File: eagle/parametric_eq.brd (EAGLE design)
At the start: 100 x 80 mm, 39 parts, among them IC1 TL072P, IC2 TL072P

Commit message: parts are on the board
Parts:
- removed LEVEL, LEVEL1, LEVEL2: 5k lin, bourns_ptd:PTD901
- added HILEV, LOLEV, MIDLEV: 5k lin, bourns_ptd:PTD901
- GAIN: value 5k -> 5k lin; device pot:3RP/1610N -> bourns_ptd:PTD901
- moved HI 197.1 mm to (87.6, 5.08)
- moved MID 161.6 mm to (62.2, 5.08)
- moved R20 156.2 mm to (81.3, 21.6)
- moved R7 150.6 mm to (80.0, 35.6)
- moved C9 149.4 mm to (74.9, 11.4)
- moved R19 147.7 mm to (81.3, 16.5)
- moved C10 142.9 mm to (66.0, 21.6)
- moved R15 139.5 mm to (59.7, 12.7)
- moved IC2 138.5 mm to (66.0, 29.2), turned to 270 degrees
- moved C8 135.7 mm to (68.6, 16.5)
- moved LOW 126.1 mm to (36.8, 5.08)
- moved R14 124.8 mm to (57.1, 16.5)
- moved C7 116.2 mm to (49.5, 11.4)
- moved C11 115.3 mm to (29.2, 21.6)
- moved C12 114.5 mm to (29.2, 38.1)
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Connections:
- net N$13: now also LOLEV.2; no longer LEVEL.2
- net N$14: now also MIDLEV.2; no longer LEVEL1.2
- net N$2: now also GAIN.1; no longer GAIN.3
- net N$21: now also HILEV.2; no longer LEVEL2.2
- net N$23: now also GAIN.3, LOLEV.1; no longer GAIN.1, LEVEL.1
- net N$6: now also LOLEV.3, MIDLEV.1; no longer LEVEL.3, LEVEL1.1
- net N$7: now also HILEV.1, MIDLEV.3; no longer LEVEL1.3, LEVEL2.1
- net N$8: now also HILEV.3; no longer LEVEL2.3

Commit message: almost routed
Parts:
- removed HI, LOW, MID: 50k log, bourns_ptd:PTD902
- added HIFREQ, LOWFREQ, MIDFREQ: 50k log, bourns_ptd:PTD902
- C1, C2, C3, C4, C5, C6, C7, C8, C9: device rcl:C025-030X050 -> rcl:C050-050X075
- moved C11 10.2 mm to (20.3, 26.7), turned to 270 degrees
- moved R12 9.25 mm to (38.1, 14.0)
- moved R10 8.98 mm to (6.35, 19.1)
- moved OUT 7.62 mm to (84.5, 55.2)
- moved C2 7.41 mm to (53.3, 38.1)
- moved R20 6.48 mm to (87.6, 22.9)
- moved C5 6.35 mm to (26.7, 16.5), turned to 0 degrees
- moved U$1 5.68 mm to (52.1, 54.6)
- moved HILEV 5.08 mm to (80.0, 5.08)
- moved C10 4.58 mm to (62.2, 24.1), turned to 180 degrees
- moved C6 4.58 mm to (49.5, 26.7)
- moved R19 4.58 mm to (85.1, 19.1)
- moved R6 4.58 mm to (47.0, 38.1)
- moved C8 4.58 mm to (71.1, 20.3), turned to 90 degrees
- moved C4 4.58 mm to (39.4, 25.4), turned to 180 degrees
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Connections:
- net N$10: now also LOWFREQ.1-3; no longer LOW.1-3
- net N$12: now also LOWFREQ.2-3; no longer LOW.2-3
- net N$16: now also MIDFREQ.2-3; no longer MID.2-3
- net N$17: now also MIDFREQ.1-3; no longer MID.1-3
- net N$18: now also HIFREQ.1-3; no longer HI.1-3
- net N$19: now also HIFREQ.2-3; no longer HI.2-3
- net N$22: now also LOWFREQ.1-1, LOWFREQ.1-2, LOWFREQ.2-1, LOWFREQ.2-2; no longer LOW.1-1, LOW.1-2, LOW.2-1, LOW.2-2
- net N$27: now also MIDFREQ.1-1, MIDFREQ.1-2, MIDFREQ.2-1, MIDFREQ.2-2; no longer MID.1-1, MID.1-2, MID.2-1, MID.2-2
- net N$28: now also HIFREQ.1-1, HIFREQ.1-2, HIFREQ.2-1, HIFREQ.2-2; no longer HI.1-1, HI.1-2, HI.2-1, HI.2-2
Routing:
- net GND: track 0.00 -> 203.2 mm
- net +12V: track 0.00 -> 153.9 mm
- net N$7: track 0.00 -> 97.9 mm
- net N$6: track 0.00 -> 79.6 mm
- net N$28: track 0.00 -> 67.1 mm
- net N$8: track 0.00 -> 64.7 mm
- net N$5: track 0.00 -> 55.7 mm
- net N$27: track 0.00 -> 39.8 mm
- net N$22: track 0.00 -> 29.7 mm
- net N$4: track 0.00 -> 26.7 mm
- net N$3: track 0.00 -> 25.2 mm
- net N$1: track 0.00 -> 24.0 mm
- net N$19: track 0.00 -> 21.3 mm
- net N$10: track 0.00 -> 18.5 mm
- net N$23: track 0.00 -> 18.4 mm
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
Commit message: routed
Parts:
- moved R10 7.62 mm to (14.0, 19.1)
- moved R20 5.39 mm to (83.8, 19.1)
- moved R19 4.02 mm to (86.4, 22.9)
- moved R12 2.84 mm to (35.6, 12.7)
- moved C11 1.80 mm to (21.6, 27.9)
- moved R14 1.80 mm to (59.7, 19.1)
- moved R7 1.27 mm to (80.0, 34.3)
- moved R13 1.27 mm to (44.5, 19.1)
- moved R16 1.27 mm to (22.9, 40.6)
- moved R2 1.27 mm to (15.2, 33.0)
- moved C1 1.27 mm to (30.5, 44.5)
- moved C9 1.27 mm to (77.5, 12.7)
- moved R6 1.27 mm to (48.3, 38.1)
- turned C13 to 180 degrees
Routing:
- net -12V: track 12.0 -> 127.0 mm, vias 0 -> 2
- net +12V: track 153.9 -> 94.2 mm, vias 0 -> 2
- net N$27: track 39.8 -> 76.3 mm
- net GND: track 203.2 -> 239.3 mm, vias 0 -> 2
- net N$23: track 18.4 -> 53.0 mm
- net N$4: track 26.7 -> 59.6 mm
- net N$28: track 67.1 -> 53.0 mm
- net N$8: track 64.7 -> 76.3 mm
- net N$5: track 55.7 -> 48.0 mm
- net N$9: track 0.00 -> 7.02 mm
- net N$19: track 21.3 -> 14.9 mm
- net N$3: track 25.2 -> 20.3 mm
- net N$20: track 10.7 -> 6.65 mm
- net N$18: track 18.2 -> 22.1 mm
- net N$2: track 9.47 -> 12.9 mm
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
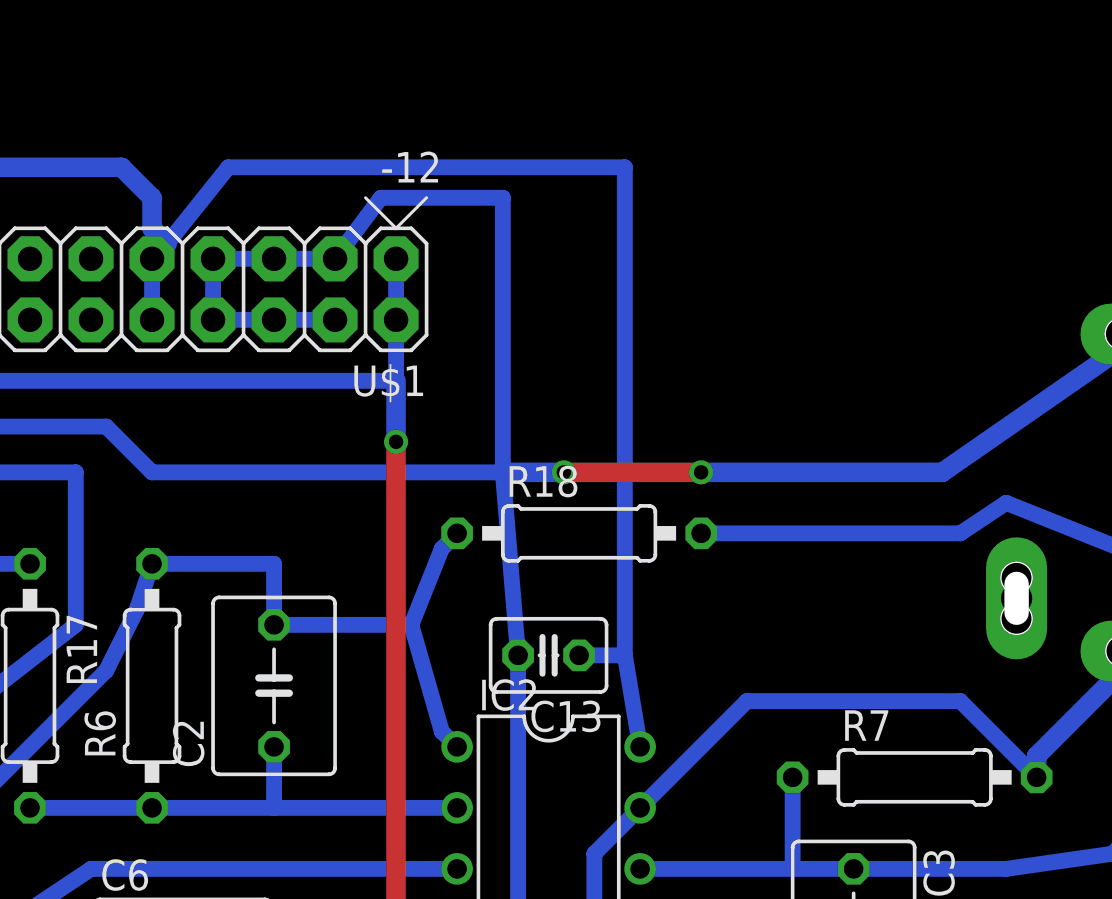
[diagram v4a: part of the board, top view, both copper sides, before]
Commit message: power filter caps
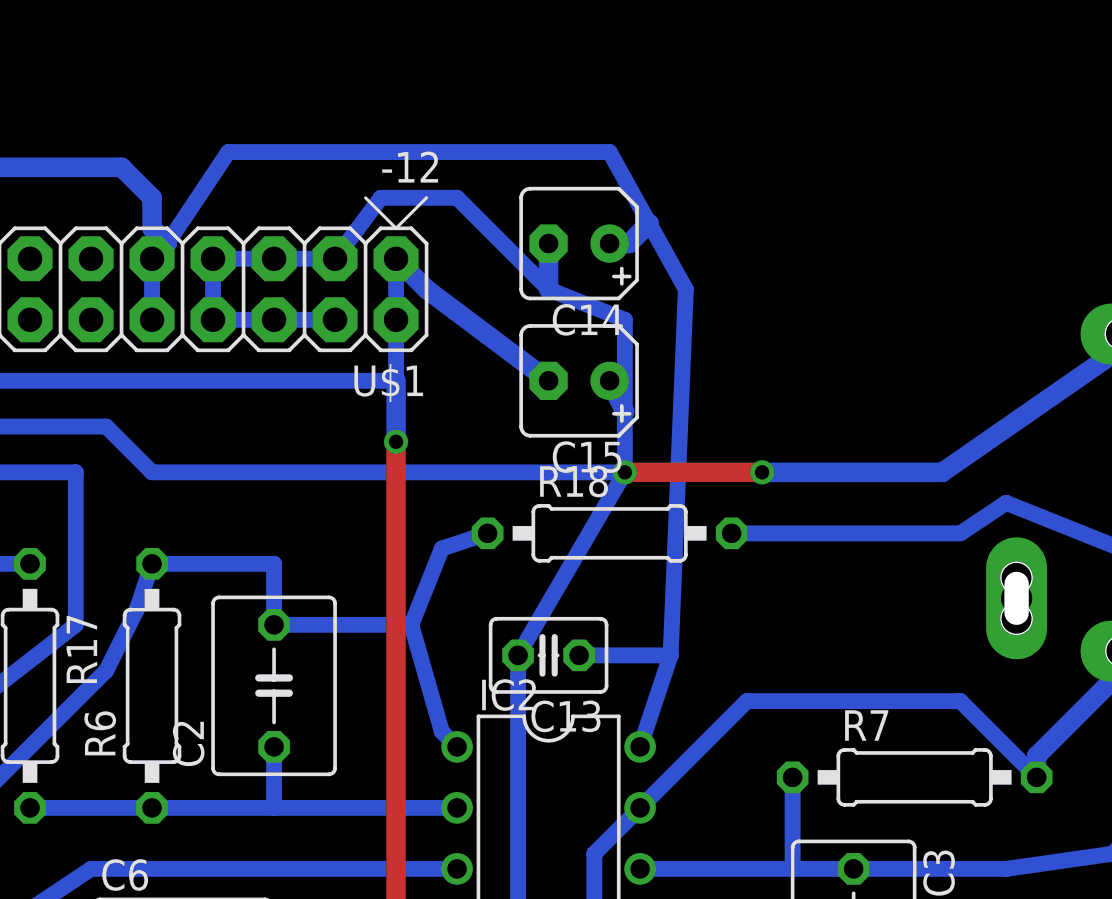
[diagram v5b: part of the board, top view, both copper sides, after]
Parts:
- added C14, C15: 10u, rcl:B45181A
- moved R18 1.27 mm to (67.3, 44.5)
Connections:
- net +12V: now also C14.+
- net -12V: now also C15.-
- net GND: now also C14.-, C15.+
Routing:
- net -12V: track 127.0 -> 135.1 mm
- net GND: track 239.3 -> 245.6 mm
- net +12V: track 94.2 -> 99.6 mm
- net N$4: track 59.6 -> 58.3 mm
- net N$7: track 95.2 -> 96.3 mm
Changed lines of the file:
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@@
 <element name="R16" library="rcl" package="0207/10" value="2k2" x="22.86" y="40.64" rot="R90"/>
 <element name="R17" library="rcl" package="0207/10" value="2k2" x="43.18" y="38.1" rot="R270"/>
-<element name="R18" library="rcl" package="0207/10" value="2k2" x="66.04" y="44.45"/>
+<element name="R18" library="rcl" package="0207/10" value="2k2" x="67.31" y="44.45"/>
 <element name="R19" library="rcl" package="0207/10" value="4k7" x="86.36" y="22.86"/>
 <element name="R2" library="rcl" package="0207/10" value="2k" x="15.24" y="33.02"/>
@@
 <element name="HILEV" library="bourns_ptd" package="PTD901" value="5k lin" x="80.01" y="5.08"/>
 <element name="GAIN" library="bourns_ptd" package="PTD901" value="5k lin" x="7.62" y="5.08"/>
+<element name="C14" library="rcl" package="B45181A" value="10u" x="66.04" y="56.515" rot="R180"/>
+<element name="C15" library="rcl" package="B45181A" value="10u" x="66.04" y="50.8" rot="R180"/>
 </elements>
 <signals>
@@
 <wire x1="77.47" y1="30.48" x2="74.93" y2="30.48" width="0.6604" layer="16"/>
 <wire x1="74.93" y1="30.48" x2="68.58" y2="30.48" width="0.6604" layer="16"/>
-<wire x1="81.915" y1="44.45" x2="71.12" y2="44.45" width="0.6604" layer="16"/>
+<wire x1="81.915" y1="44.45" x2="72.39" y2="44.45" width="0.6604" layer="16"/>
 <wire x1="83.82" y1="45.72" x2="81.915" y2="44.45" width="0.6604" layer="16"/>
 <wire x1="93.345" y1="41.91" x2="83.82" y2="45.72" width="0.6604" layer="16"/>
@@
 <wire x1="60.325" y1="43.815" x2="59.055" y2="40.64" width="0.6604" layer="16"/>
 <wire x1="59.055" y1="40.64" x2="60.325" y2="36.195" width="0.6604" layer="16"/>
-<wire x1="60.96" y1="44.45" x2="60.325" y2="43.815" width="0.6604" layer="16"/>
+<wire x1="62.23" y1="44.45" x2="60.325" y2="43.815" width="0.6604" layer="16"/>
 <wire x1="53.34" y1="43.18" x2="48.26" y2="43.18" width="0.6604" layer="16"/>
 <wire x1="53.34" y1="40.64" x2="53.34" y2="43.18" width="0.6604" layer="16"/>
@@
 <contactref element="U$1" pad="10"/>
 <wire x1="48.26" y1="55.88" x2="48.26" y2="53.34" width="0.6604" layer="16"/>
-<wire x1="67.945" y1="39.37" x2="66.04" y2="39.37" width="0.6604" layer="16"/>
-<wire x1="51.435" y1="59.69" x2="48.895" y2="56.515" width="0.6604" layer="16"/>
+<wire x1="69.85" y1="39.37" x2="66.04" y2="39.37" width="0.6604" layer="16"/>
+<wire x1="51.435" y1="60.325" x2="48.895" y2="56.515" width="0.6604" layer="16"/>
 <wire x1="48.895" y1="56.515" x2="48.26" y2="55.88" width="0.6604" layer="16"/>
-<wire x1="67.945" y1="59.69" x2="51.435" y2="59.69" width="0.6604" layer="16"/>
-<wire x1="68.58" y1="35.56" x2="67.945" y2="39.37" width="0.6604" layer="16"/>
-<wire x1="67.945" y1="39.37" x2="67.945" y2="59.69" width="0.6604" layer="16"/>
+<wire x1="70.485" y1="54.61" x2="68.95740625" y2="57.35966875" width="0.6604" layer="16"/>
+<wire x1="68.95740625" y1="57.35966875" x2="67.31" y2="60.325" width="0.6604" layer="16"/>
+<wire x1="67.31" y1="60.325" x2="51.435" y2="60.325" width="0.6604" layer="16"/>
+<wire x1="68.58" y1="35.56" x2="69.85" y2="39.37" width="0.6604" layer="16"/>
+<wire x1="69.85" y1="39.37" x2="70.485" y2="54.61" width="0.6604" layer="16"/>
 <wire x1="30.48" y1="36.83" x2="33.02" y2="34.29" width="0.6604" layer="16"/>
 <wire x1="30.48" y1="39.37" x2="30.48" y2="36.83" width="0.6604" layer="16"/>
@@
 <wire x1="48.26" y1="58.42" x2="48.26" y2="57.15" width="0.8128" layer="16"/>
 <wire x1="48.26" y1="57.15" x2="48.895" y2="56.515" width="0.8128" layer="16"/>
+<contactref element="C14" pad="+"/>
+<wire x1="67.31" y1="56.515" x2="68.1127375" y2="56.515" width="0.8128" layer="16"/>
+<wire x1="68.1127375" y1="56.515" x2="68.95740625" y2="57.35966875" width="0.8128" layer="16"/>
 </signal>
 <signal name="-12V">
@@
 <via x="58.42" y="48.26" extent="1-16" drill="0.6" shape="square"/>
 <wire x1="58.42" y1="48.26" x2="58.42" y2="50.8" width="0.8128" layer="16"/>
+<contactref element="C15" pad="-"/>
+<wire x1="64.77" y1="50.8" x2="59.69" y2="54.61" width="0.8128" layer="16"/>
+<wire x1="59.69" y1="54.61" x2="58.42" y2="55.88" width="0.8128" layer="16"/>
 </signal>
 <signal name="GND">
@@
 <wire x1="63.5" y1="24.13" x2="63.5" y2="39.37" width="0.6604" layer="16"/>
 <wire x1="57.785" y1="58.42" x2="55.88" y2="55.88" width="0.6604" layer="16"/>
-<wire x1="62.865" y1="58.42" x2="57.785" y2="58.42" width="0.6604" layer="16"/>
-<wire x1="63.5" y1="39.37" x2="62.865" y2="46.99" width="0.6604" layer="16"/>
-<wire x1="62.865" y1="46.99" x2="62.865" y2="58.42" width="0.6604" layer="16"/>
+<wire x1="67.945" y1="53.34" x2="64.77" y2="54.61" width="0.6604" layer="16"/>
+<wire x1="64.77" y1="54.61" x2="60.96" y2="58.42" width="0.6604" layer="16"/>
+<wire x1="60.96" y1="58.42" x2="57.785" y2="58.42" width="0.6604" layer="16"/>
+<wire x1="63.5" y1="39.37" x2="67.945" y2="46.99" width="0.6604" layer="16"/>
+<wire x1="67.945" y1="46.99" x2="67.945" y2="49.53" width="0.6604" layer="16"/>
+<wire x1="67.945" y1="49.53" x2="67.945" y2="53.34" width="0.6604" layer="16"/>
 <wire x1="47.625" y1="26.67" x2="46.99" y2="26.67" width="0.6604" layer="16"/>
 <wire x1="51.435" y1="28.575" x2="47.625" y2="26.67" width="0.6604" layer="16"/>
@@
 <wire x1="19.685" y1="46.355" x2="19.685" y2="39.37" width="0.6604" layer="16"/>
 <wire x1="22.225" y1="48.895" x2="19.685" y2="46.355" width="0.6604" layer="16"/>
-<wire x1="62.865" y1="46.99" x2="48.26" y2="46.99" width="0.6604" layer="16"/>
+<wire x1="67.945" y1="46.99" x2="48.26" y2="46.99" width="0.6604" layer="16"/>
 <wire x1="48.26" y1="46.99" x2="46.355" y2="48.895" width="0.6604" layer="16"/>
 <wire x1="46.355" y1="48.895" x2="22.225" y2="48.895" width="0.6604" layer="16"/>
-<wire x1="62.865" y1="46.99" x2="65.405" y2="46.99" width="0.8128" layer="16"/>
-<via x="65.405" y="46.99" extent="1-16" drill="0.6" shape="square"/>
-<wire x1="65.405" y1="46.99" x2="71.12" y2="46.99" width="0.8128" layer="1"/>
-<via x="71.12" y="46.99" extent="1-16" drill="0.6" shape="square"/>
-<wire x1="71.12" y1="46.99" x2="81.16" y2="46.99" width="0.8128" layer="16"/>
+<via x="67.945" y="46.99" extent="1-16" drill="0.6" shape="square"/>
+<wire x1="67.945" y1="46.99" x2="73.66" y2="46.99" width="0.8128" layer="1"/>
+<via x="73.66" y="46.99" extent="1-16" drill="0.6" shape="square"/>
+<wire x1="73.66" y1="46.99" x2="81.16" y2="46.99" width="0.8128" layer="16"/>
 <wire x1="81.16" y1="46.99" x2="89.455" y2="52.745" width="0.8128" layer="16"/>
 <wire x1="11.985" y1="52.745" x2="17.105" y2="52.745" width="0.8128" layer="16"/>
 <wire x1="17.105" y1="52.745" x2="22.225" y2="48.895" width="0.8128" layer="16"/>
+<contactref element="C14" pad="-"/>
+<contactref element="C15" pad="+"/>
+<wire x1="67.31" y1="50.8" x2="67.945" y2="49.53" width="0.8128" layer="16"/>
+<wire x1="64.77" y1="56.515" x2="64.77" y2="54.61" width="0.8128" layer="16"/>
 </signal>
 <signal name="N$22">
